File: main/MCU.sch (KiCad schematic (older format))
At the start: 14 parts

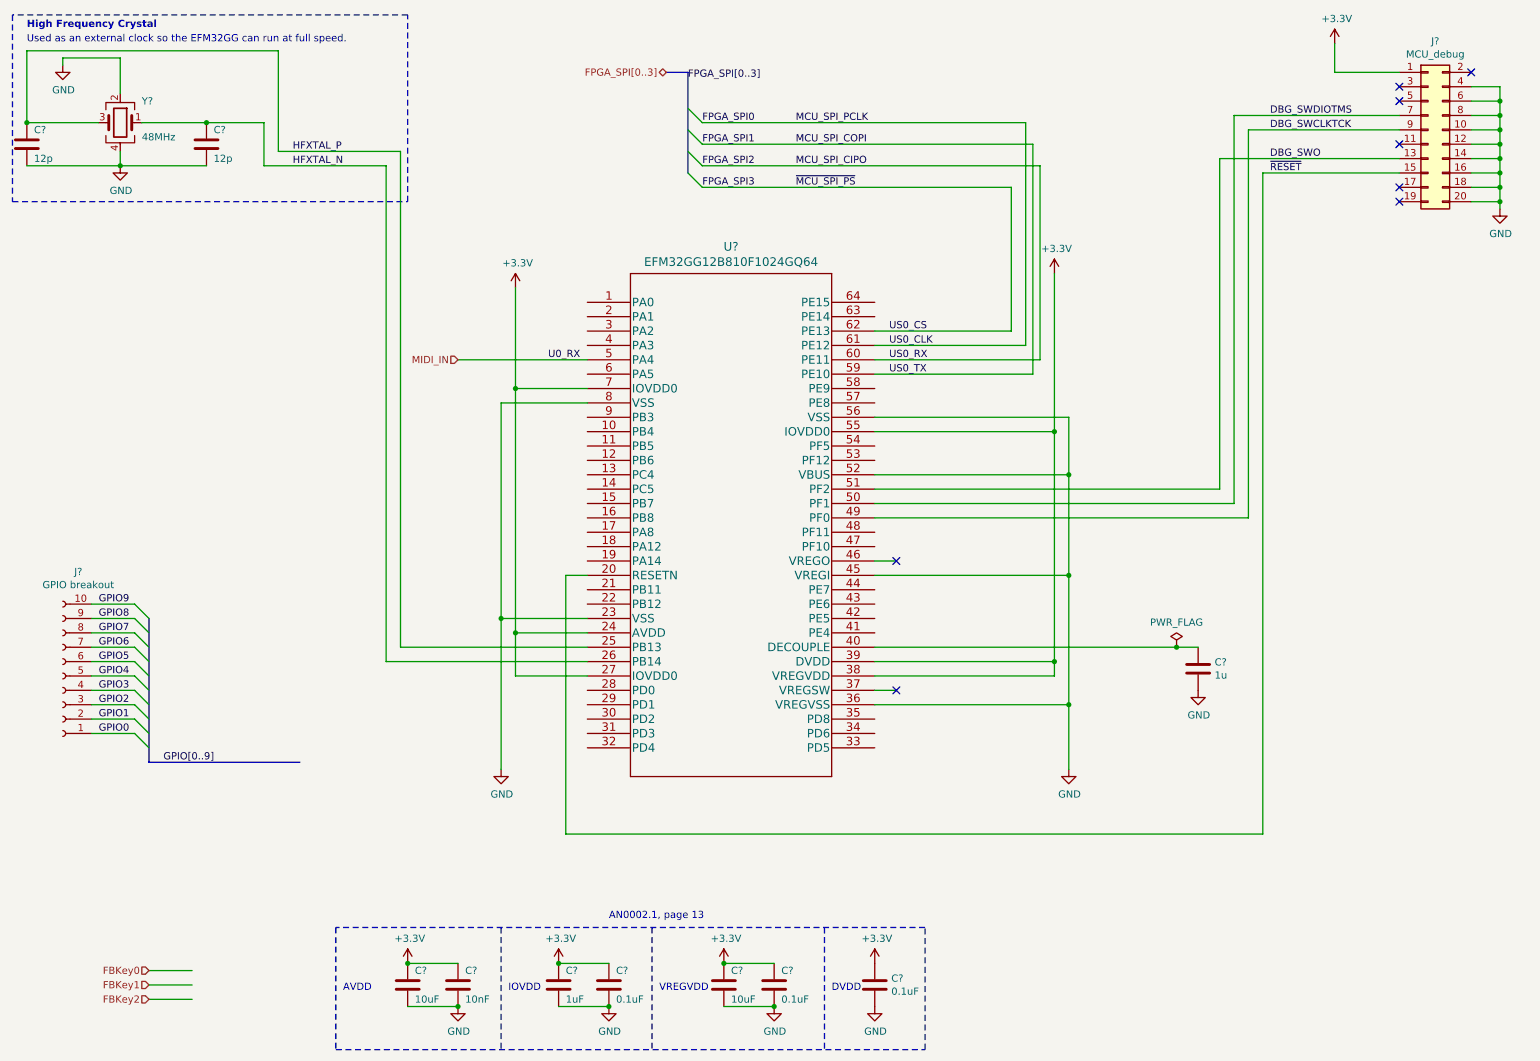
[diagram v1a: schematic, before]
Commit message: Set up switching regulator circuits.
We only use half of the switching regulator that generates the 1V0
voltage. I'm not sure if the half not being used is connected correctly.
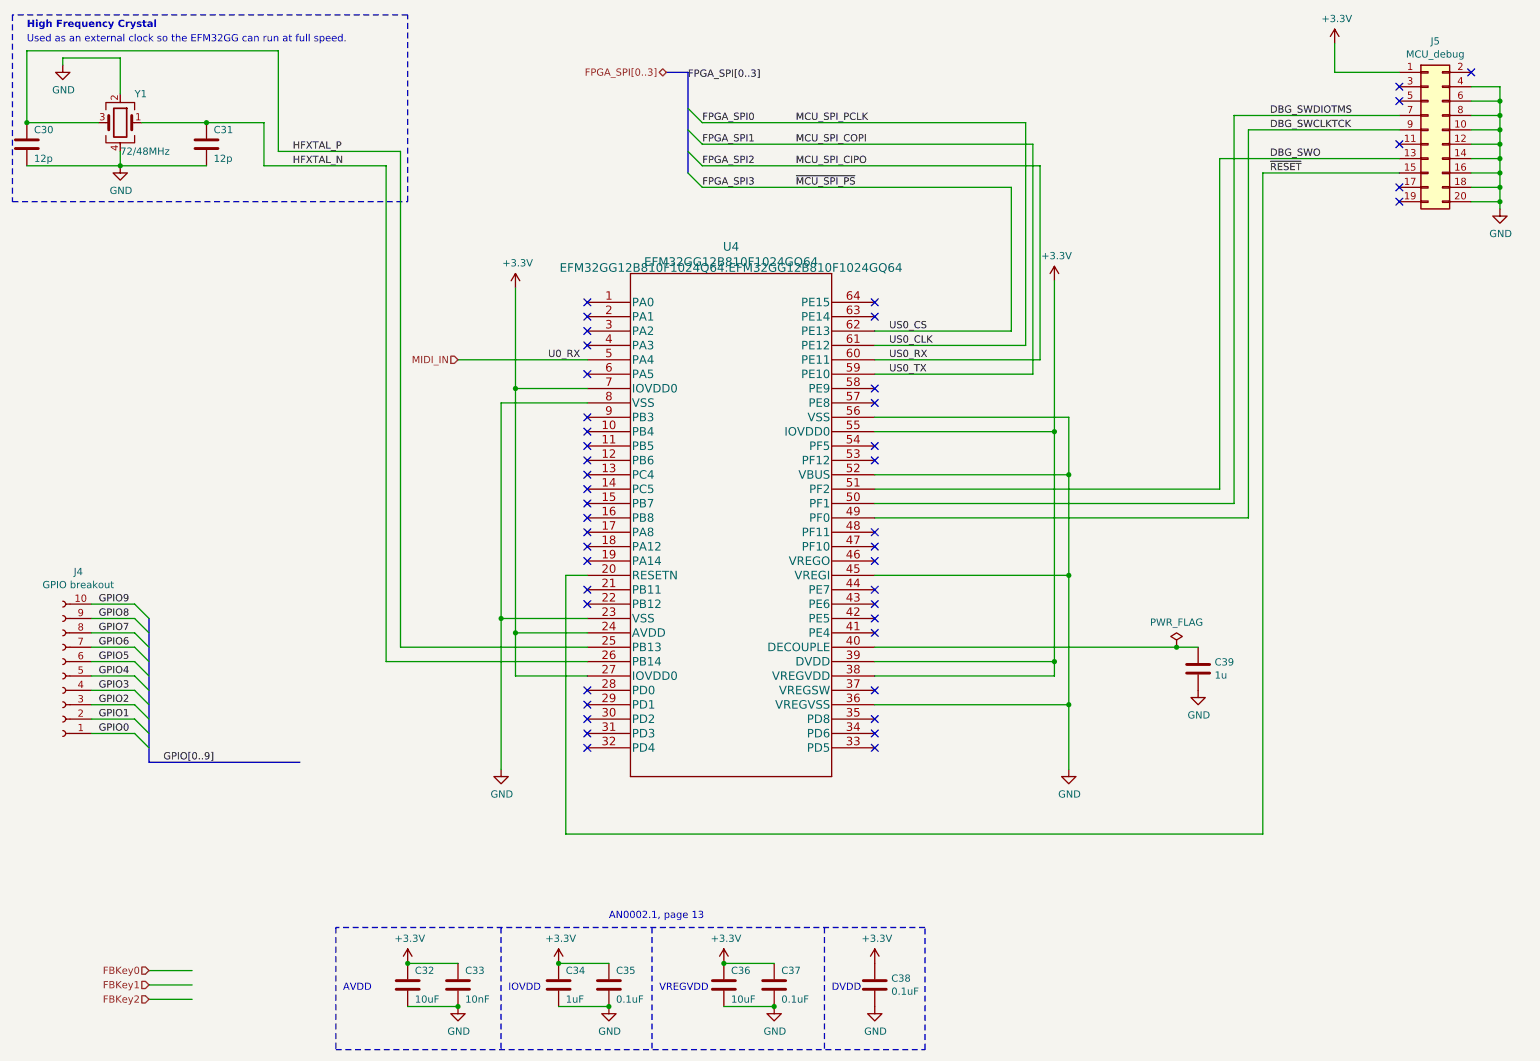
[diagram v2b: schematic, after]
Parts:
- U4: renamed from U?; footprint TQFP64_10X10_SIL -> EFM32GG12B810F1024Q64:EFM32GG12B810F1024GQ64
- Y1: renamed from Y?; value 48MHz -> 72/48MHz
- gave numbers to parts that had none: 12
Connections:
- no-connect marks 8 -> 46

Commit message: Continue wiring of the MCU
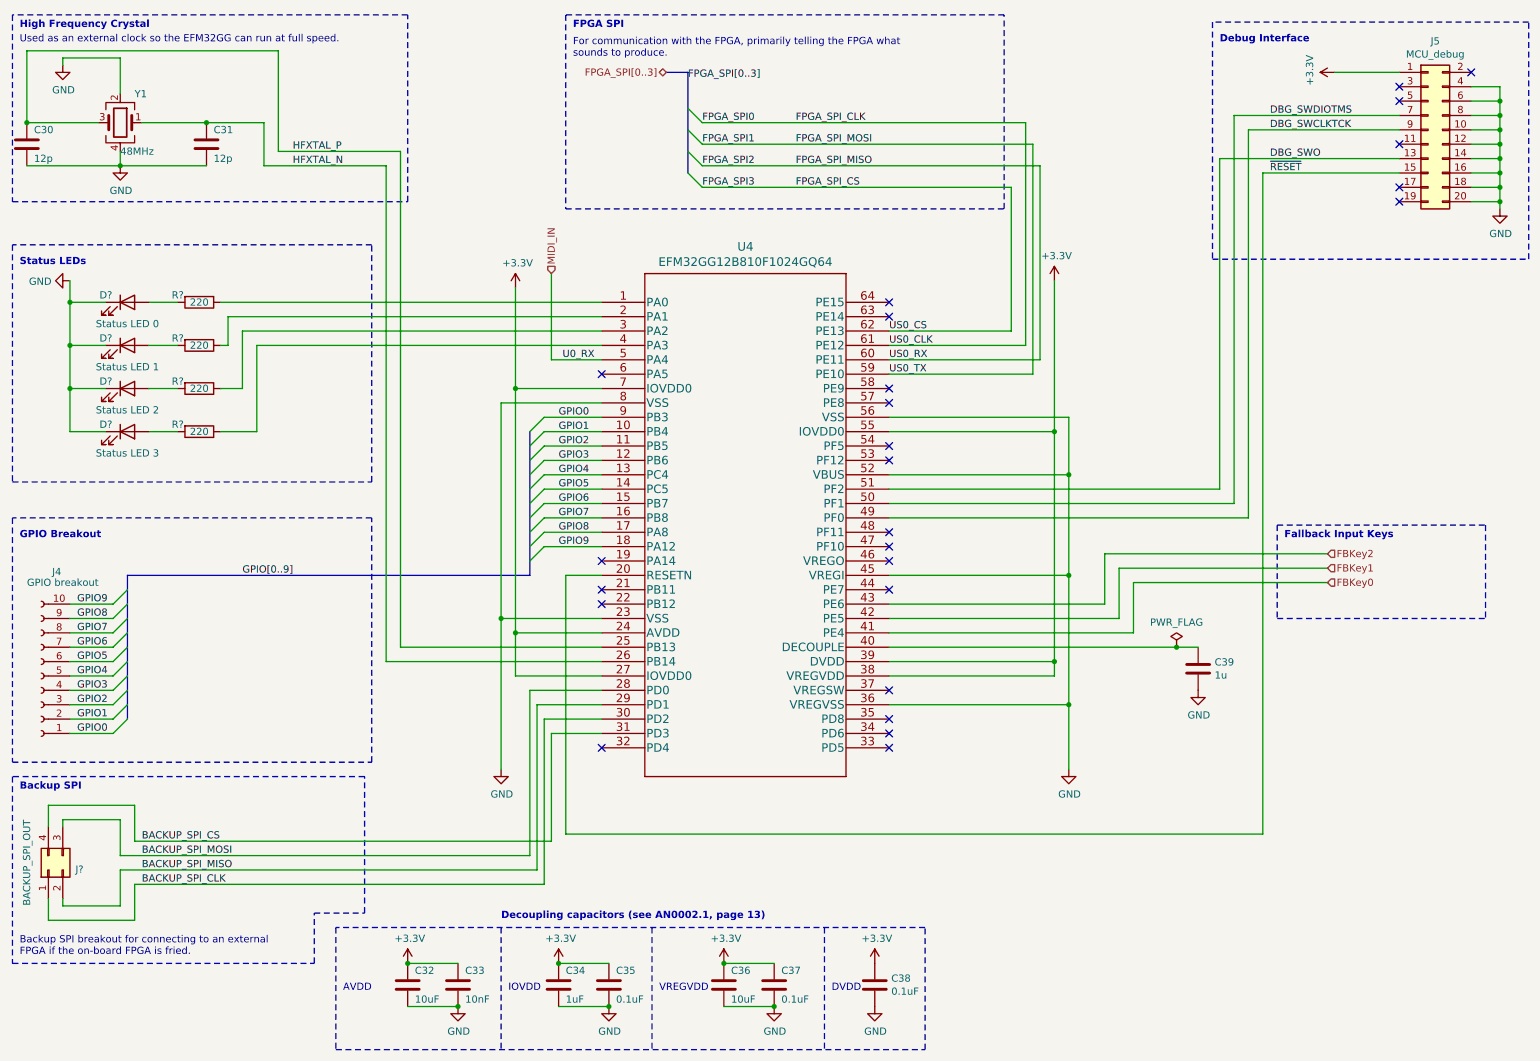
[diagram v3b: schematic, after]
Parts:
- added D?: Status LED 3, symbol Device:LED
- added D?: Status LED 2, symbol Device:LED
- added D?: Status LED 1, symbol Device:LED
- added D?: Status LED 0, symbol Device:LED
- added J?: BACKUP_SPI_OUT, symbol Connector_Generic:Conn_02x02_Counter_Clockwise
- added R? (x4): 220, symbol Device:R
- Y1: value 72/48MHz -> 48MHz
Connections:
- net FBKey0: now also U4.41 (PE4)
- net FBKey1: now also U4.42 (PE5)
- net FBKey2: now also U4.43 (PE6)
- net GND: now also D?.1 (K), D?.1 (K), D?.1 (K), D?.1 (K)
- net GPIO0: now also U4.9 (PB3)
- net GPIO1: now also U4.10 (PB4)
- net GPIO2: now also U4.11 (PB5)
- net GPIO3: now also U4.12 (PB6)
- net GPIO4: now also U4.13 (PC4)
- net GPIO5: now also U4.14 (PC5)
- net GPIO6: now also U4.15 (PB7)
- net GPIO7: now also U4.16 (PB8)
- net GPIO8: now also U4.17 (PA8)
- net GPIO9: now also U4.18 (PA12)
- net at U4.1 (PA0): now also R?.1
- net at U4.2 (PA1): now also R?.1
- net BACKUP_SPI_MOSI: now reaches U4.28 (PD0)
- net BACKUP_SPI_MOSI: now also J?.3 (Pin_3)
- net BACKUP_SPI_MISO: now reaches U4.29 (PD1)
- net BACKUP_SPI_MISO: now also J?.2 (Pin_2)
- net at U4.3 (PA2): now also R?.1
- net BACKUP_SPI_CLK: now reaches U4.30 (PD2)
- net BACKUP_SPI_CLK: now also J?.1 (Pin_1)
- net BACKUP_SPI_CS: now reaches U4.31 (PD3)
- net BACKUP_SPI_CS: now also J?.4 (Pin_4)
- net at U4.4 (PA3): now also R?.1
- new net: D?.2 (A), R?.2 (x4)
- no-connect marks 46 -> 25
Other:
- note added: "Backup SPI"
- note added: "Backup SPI breakout for connecting to an external\nFPGA if the on-board FPGA is fried.\n"
- note added: "Debug Interface"
- note added: "Decoupling capacitors (see AN0002.1, page 13)"
- note added: "FPGA SPI"
- note added: "Fallback Input Keys"
- note added: "For communication with the FPGA, primarily telling the FPGA what\nsounds to produce."
- note added: "GPIO Breakout"
- note added: "Status LEDs"
- note removed: "AN0002.1, page 13"
- moved on the sheet: J4, U4
